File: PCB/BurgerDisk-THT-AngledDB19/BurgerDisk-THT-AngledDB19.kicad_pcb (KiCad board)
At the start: 2 copper layers, 93.7 x 73.4 mm, 17 parts, among them J1 Daisy port in, J2 MicroSD module, J3 UART, J4 Daisy port out, U1 PC817

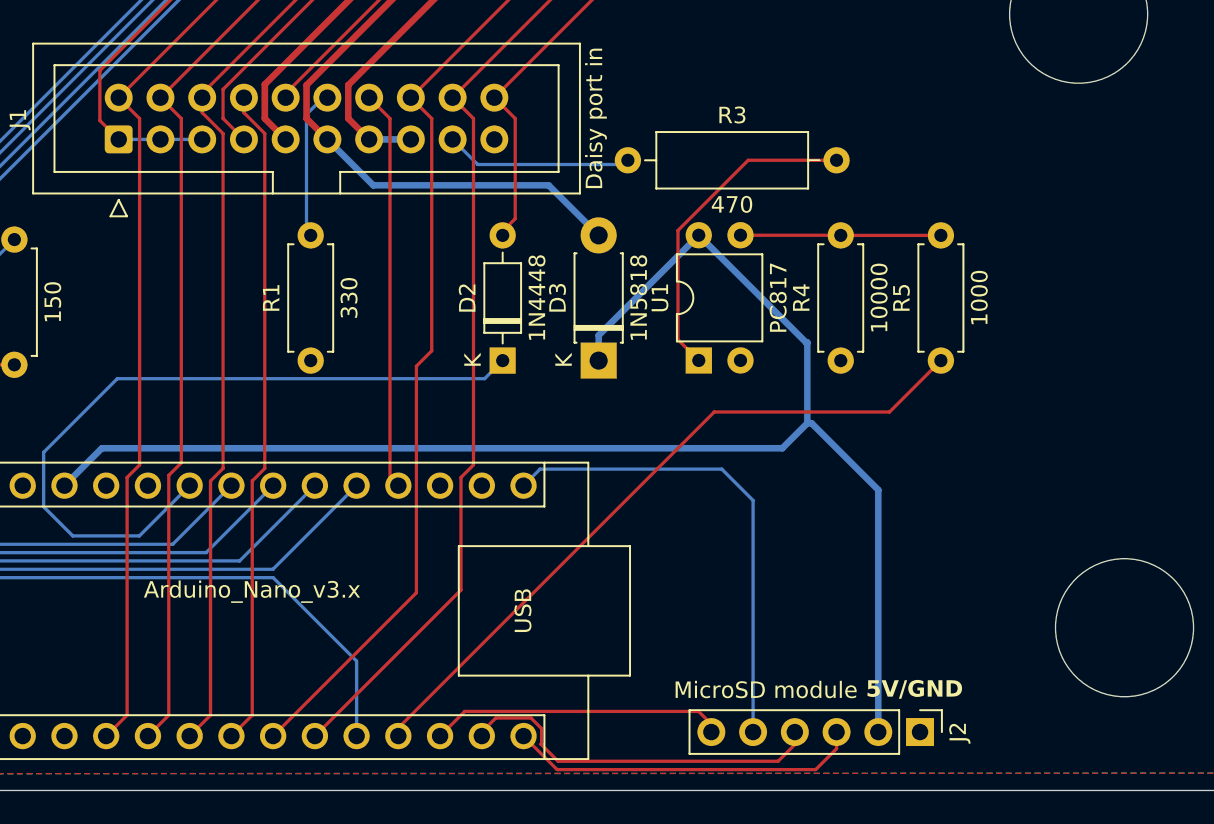
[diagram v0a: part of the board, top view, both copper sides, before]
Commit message: Rework R3 so everything's in line
for easier soldering
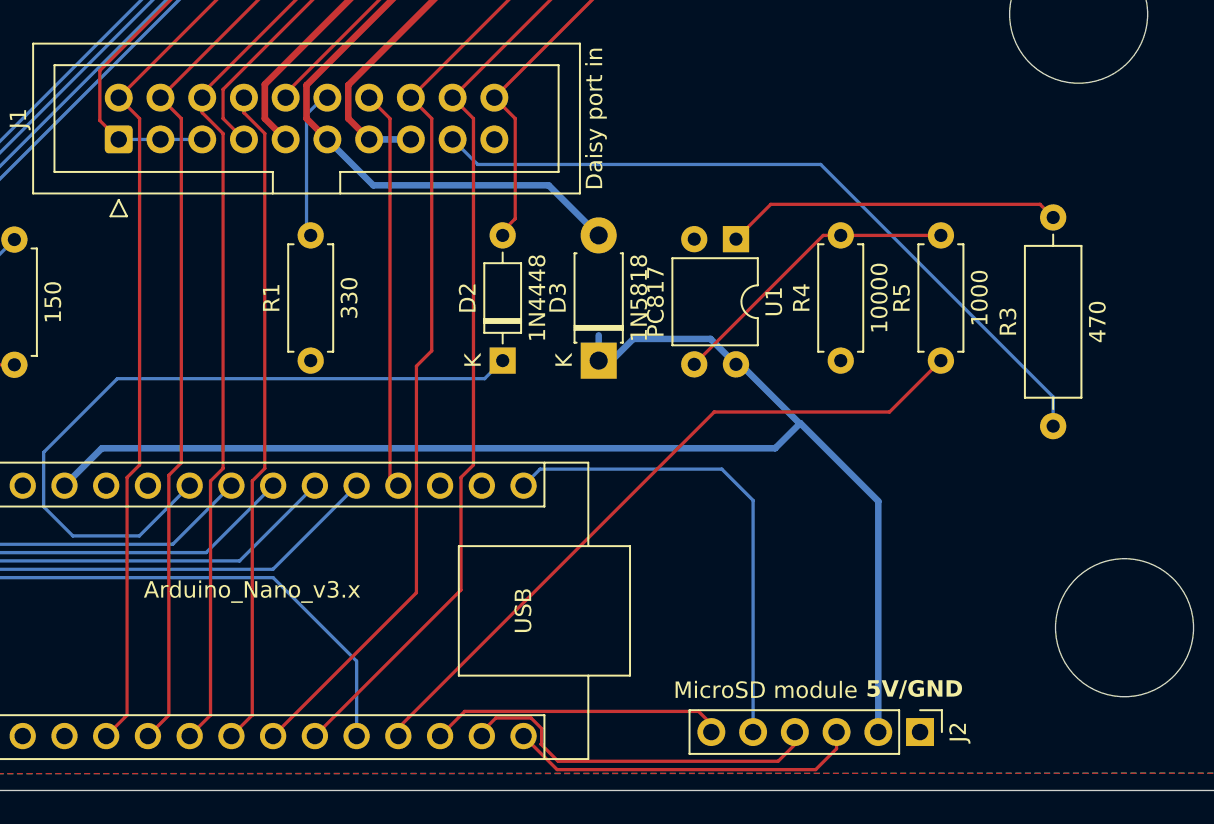
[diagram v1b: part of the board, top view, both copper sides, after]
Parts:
- moved R3 30.5 mm to (152.6, 89.1), turned to 90 degrees
- moved U1 7.72 mm to (133.3, 77.7), turned to -90 degrees
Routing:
- net DRV2_in: track 11.4 -> 44.8 mm
- net 5V_burgerDisk: track 91.9 -> 83.6 mm
- net Net-(R4-Pad2): track 12.2 -> 18.3 mm
- net Net-(R3-Pad2): track 19.9 -> 20.5 mm

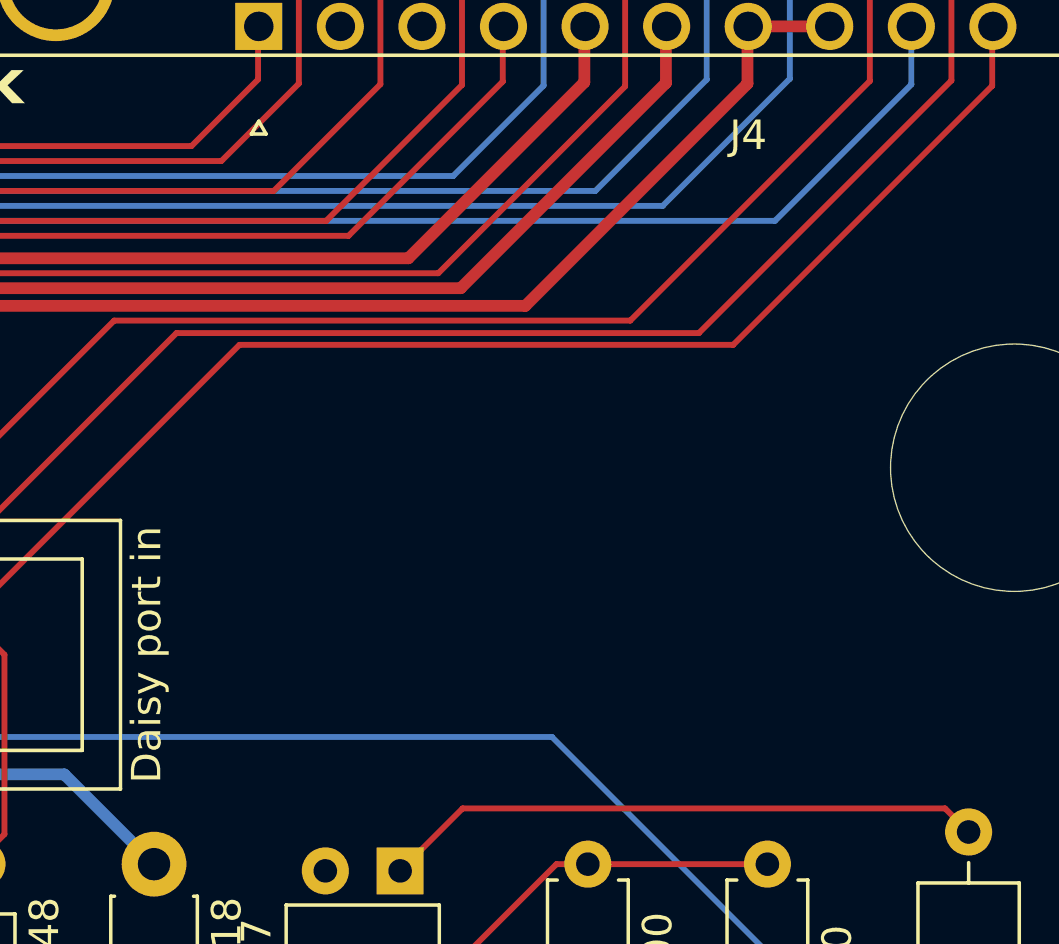
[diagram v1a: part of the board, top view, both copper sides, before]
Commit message: Add logo (thanks to Javier Rivera!!)
Add my own micro/SD modules
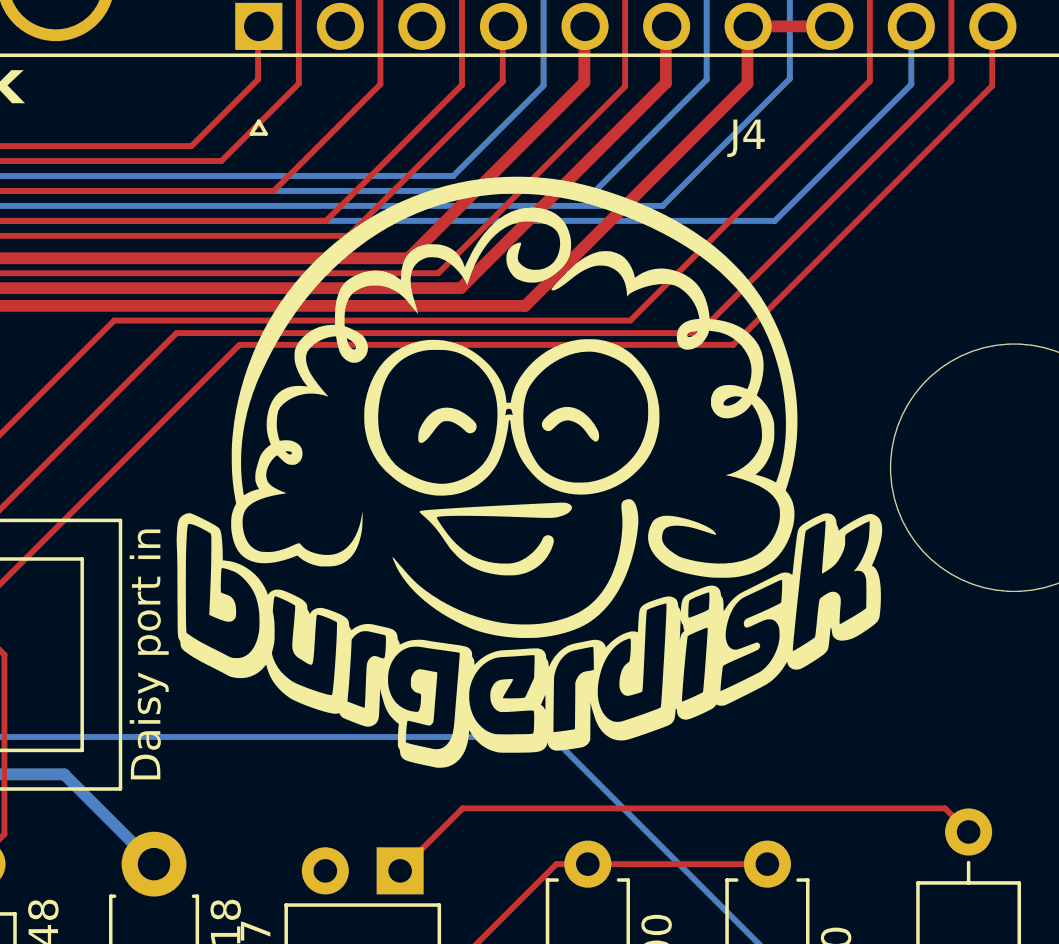
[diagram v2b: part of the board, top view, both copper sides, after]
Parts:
- added G***: LOGO, LOGO, F.Cu at (137.7, 64.2)

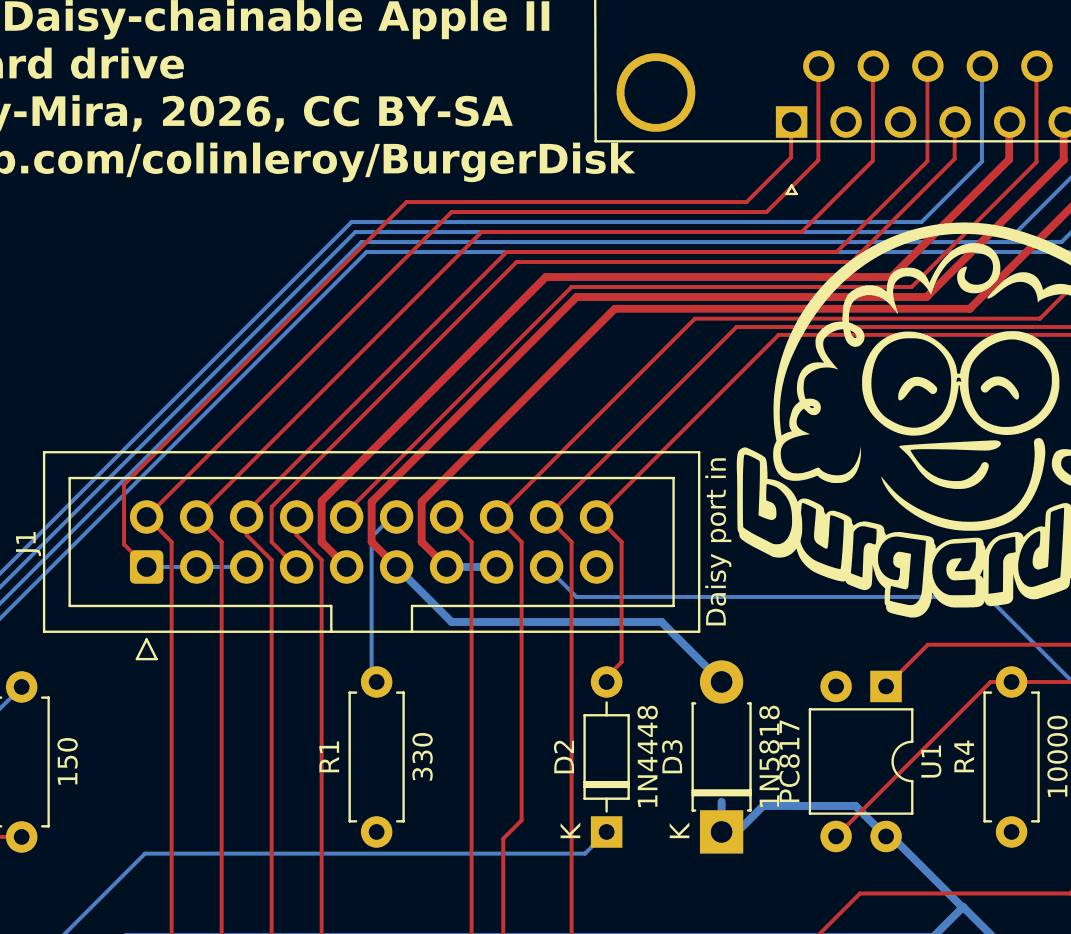
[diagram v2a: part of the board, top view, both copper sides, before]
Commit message: Enable teardrops
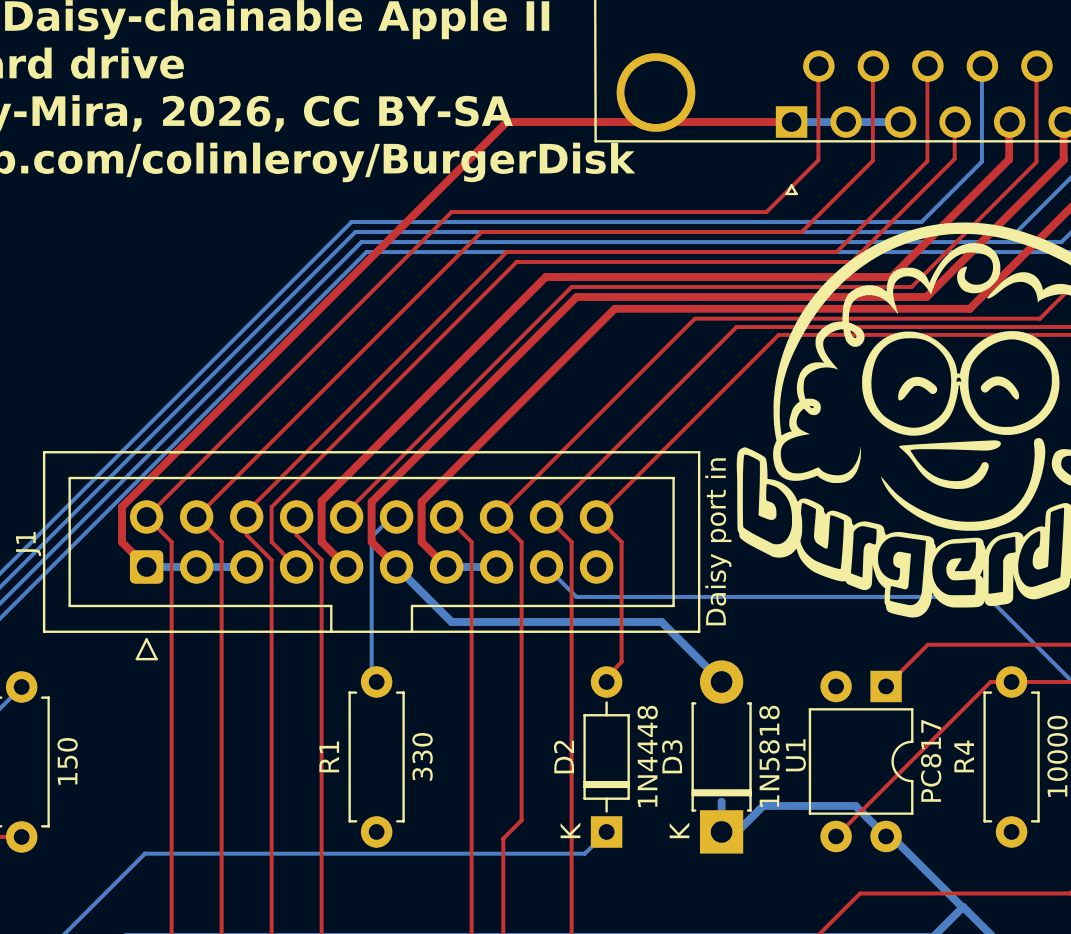
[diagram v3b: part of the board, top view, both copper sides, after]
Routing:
- net GND: track 53.1 -> 57.0 mm

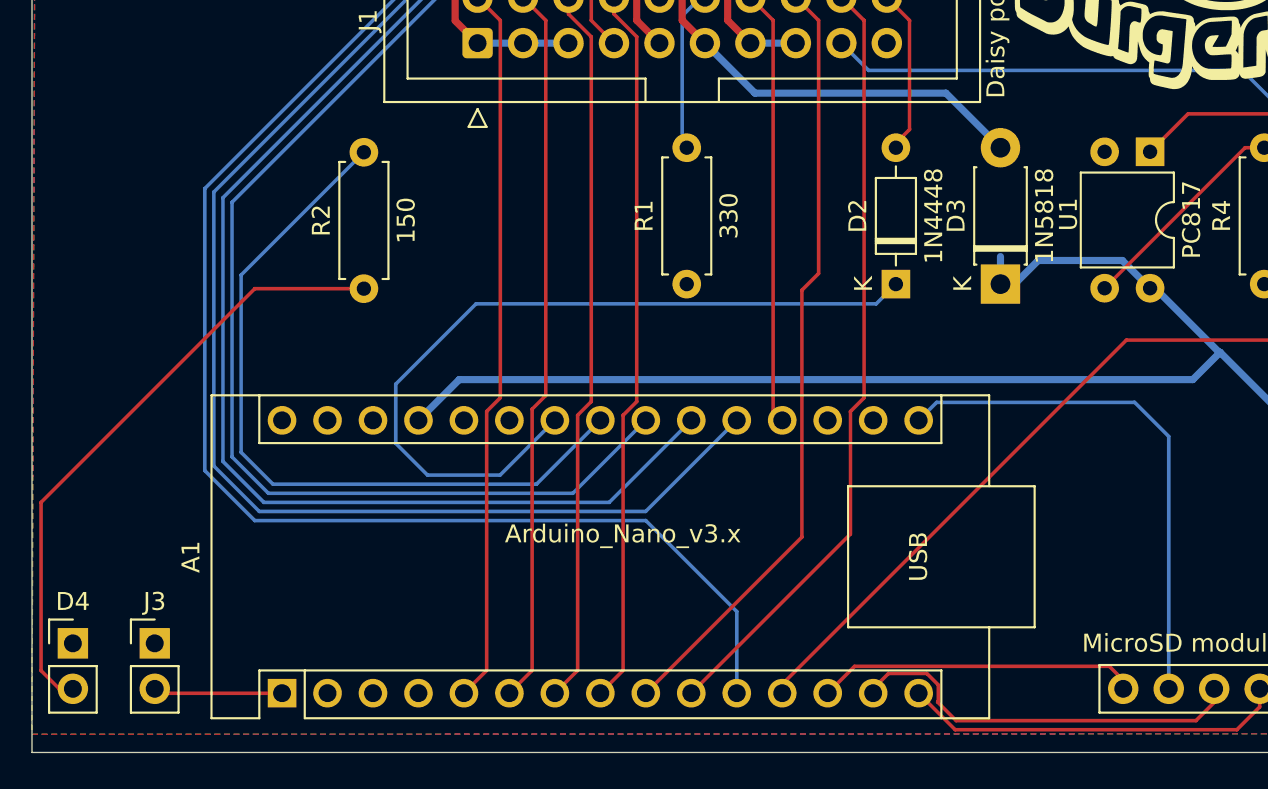
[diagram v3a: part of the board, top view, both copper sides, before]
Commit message: Add indicator on PC817 pin1
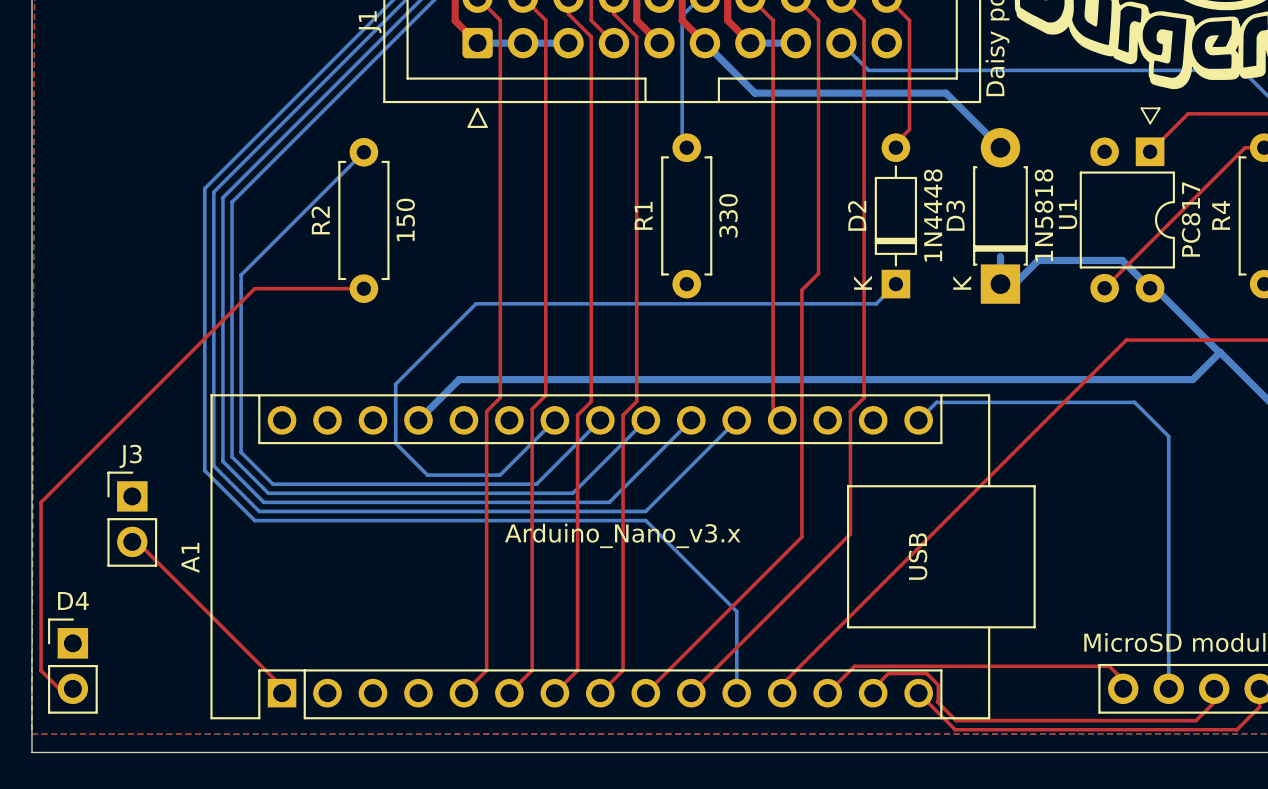
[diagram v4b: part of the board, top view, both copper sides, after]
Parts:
- moved J3 8.30 mm to (76.5, 96.9)
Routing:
- net TX: track 7.22 -> 12.1 mm

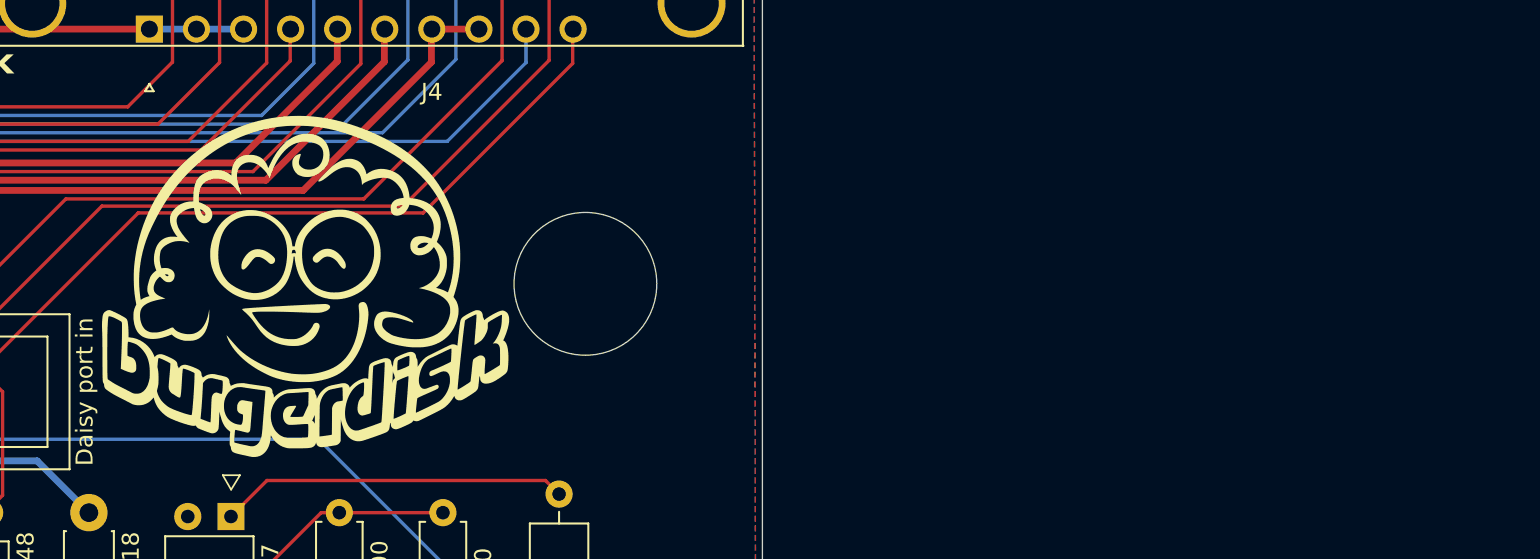
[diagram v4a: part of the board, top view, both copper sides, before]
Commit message: Move logo out of PCB
until I'm sure Rebecca's estate is OK with it
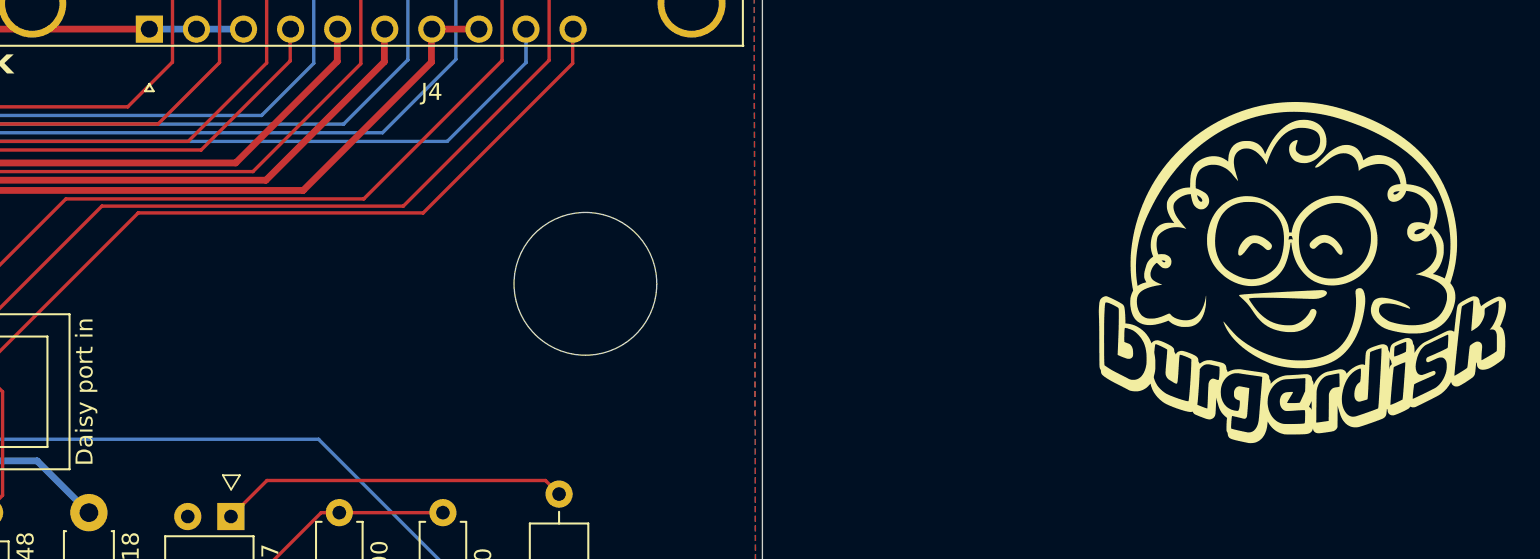
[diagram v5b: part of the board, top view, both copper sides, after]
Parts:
- moved G*** 58.7 mm to (196.3, 63.4)
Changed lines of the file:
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@@
 	(footprint "LOGO"
 		(layer "F.Cu")
-		(at 137.6934 64.2366)
+		(at 196.34 63.42)
 		(property "Reference" "G***"
 			(at 0 0 0)

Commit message: OCD
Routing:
- net SCK: track 29.3 -> 20.8 mm
- net 5V_burgerDisk: track 83.6 -> 79.8 mm
- net MOSI: track 22.5 -> 20.4 mm
- net MISO: track 21.4 -> 20.9 mm
- net GND: vias 0 -> 31

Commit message: Better grounds
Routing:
- net DRV1_out: track 125.6 -> 123.4 mm
- net HDSEL_out: track 127.1 -> 125.0 mm
- net 5V_apple2: track 67.1 -> 66.1 mm
- net WREQ: track 47.9 -> 47.1 mm
- net GND: vias 31 -> 33
